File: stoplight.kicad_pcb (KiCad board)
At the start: 4 copper layers, 18.5 x 30.2 mm, 45 parts, among them J1 Conn_01x04_Socket, Q1 DOZ30P03, U1 HUSB238_002DD, U3 TMC2209-LA-T, U4 DS18B20U, U5 TPS54202DDCR

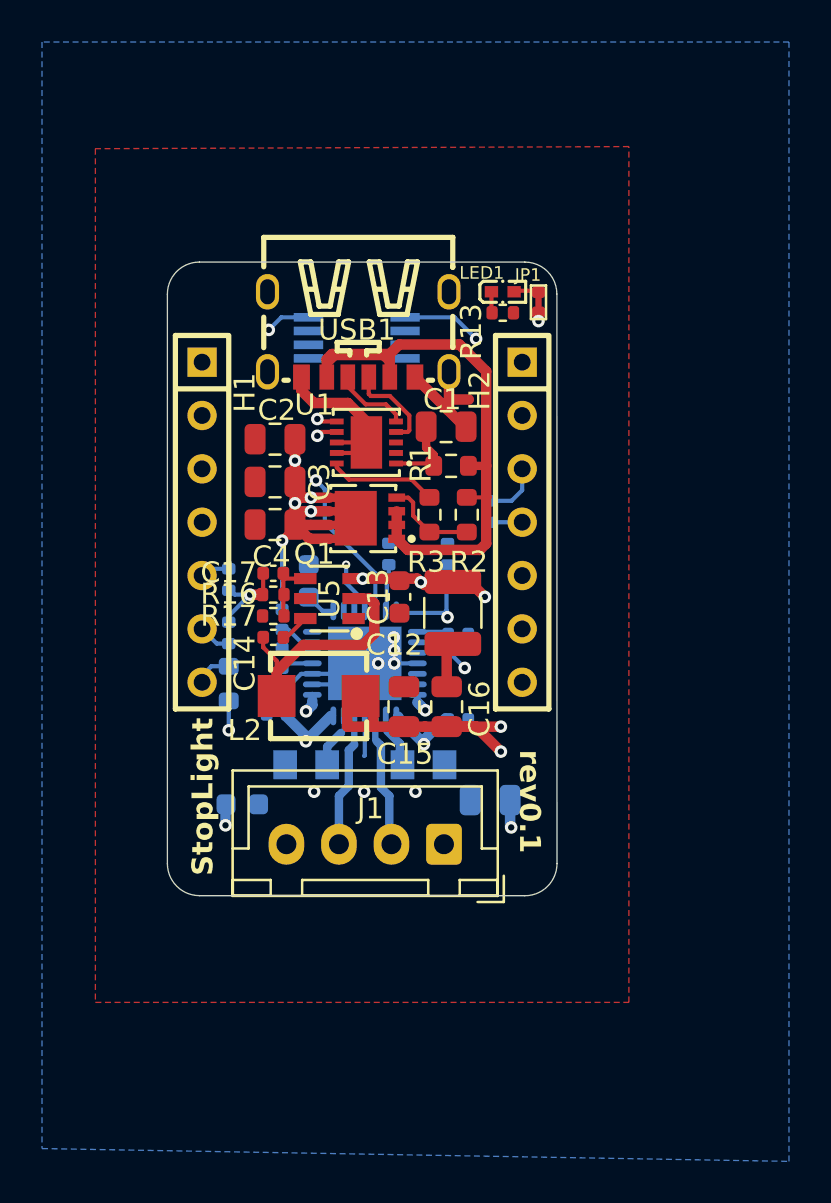
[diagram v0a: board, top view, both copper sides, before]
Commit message: add power pours and additional vias
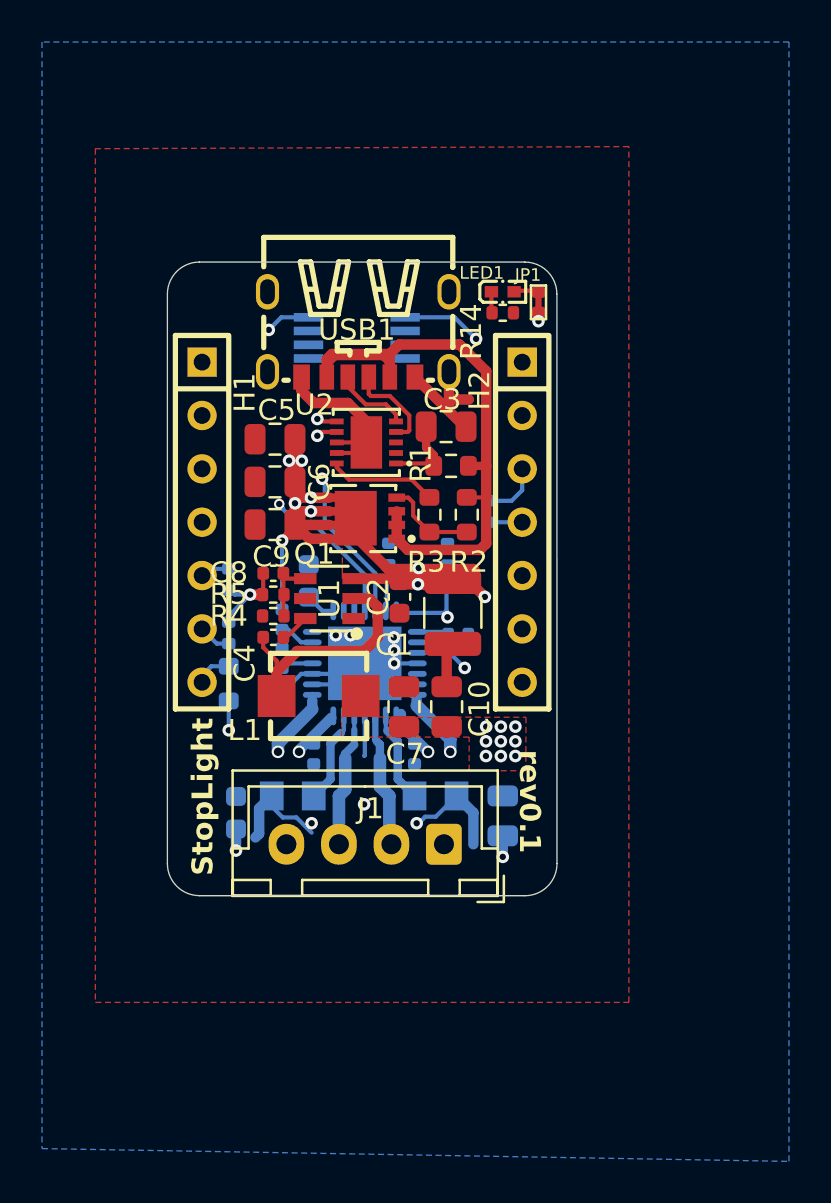
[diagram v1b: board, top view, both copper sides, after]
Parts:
- moved C16 2.64 mm to (152.6, 90.0), turned to 90 degrees
- moved C15 2.58 mm to (147.8, 90.0), turned to 90 degrees
- moved R8 1.62 mm to (146.8, 92.0)
- moved R9 1.59 mm to (153.6, 92.0)
- moved C18 0.96 mm to (156.8, 93.0), turned to -90 degrees
- moved C14 0.50 mm to (144.1, 92.8), turned to -90 degrees
- renumbered C12 to C1, C16 to C10, C6 to C11, C7 to C12, C5 to C13, C8 to C14, C9 to C15, C10 to C16, C11 to C17, C13 to C2, C1 to C3, C14 to C4, C2 to C5, C3 to C6, C15 to C7, C17 to C8, C4 to C9, L2 to L1, R8 to R10, R9 to R11, R10 to R12, R11 to R13, R13 to R14, R17 to R4, R16 to R5, R4 to R6, R5 to R7, R6 to R8, R7 to R9, U5 to U1, U1 to U2
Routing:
- net +3V3: track 26.7 -> 14.1 mm, vias 6 -> 13
- net /DIAG: track 11.3 -> 21.3 mm
- net GND: track 31.4 -> 41.3 mm, vias 7 -> 8
- net VM: track 33.9 -> 41.5 mm, vias 12 -> 13
- net Net-(U3-BRA): track 2.48 -> 4.38 mm
- net Net-(U3-BRB): track 3.07 -> 4.40 mm
- net /INDEX: track 17.2 -> 18.0 mm
- added copper zone on F.Cu, net +3V3
- added copper zone on F.Cu, net VM
